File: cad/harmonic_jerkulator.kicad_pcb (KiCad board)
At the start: 2 copper layers, 91 x 87 mm, 43 parts, among them J101 JACK_IN, J102 JACK_OUT, J103 CONN_PSU, J105 PNP, J106 NPN, J107 SW_BYPASS, J108 DIODE1, J109 SW_DIODE, J110 DIODE2, J111 CONN_CONN_BOARD, J112 SW_DIODE, J113 CONN_CIRCUIT_BOARD, K101 TQ2SA-5V, Q101 BC850, Q102 BC856, Q103 DTC123Y, Q104 DTC123Y, U101 4013

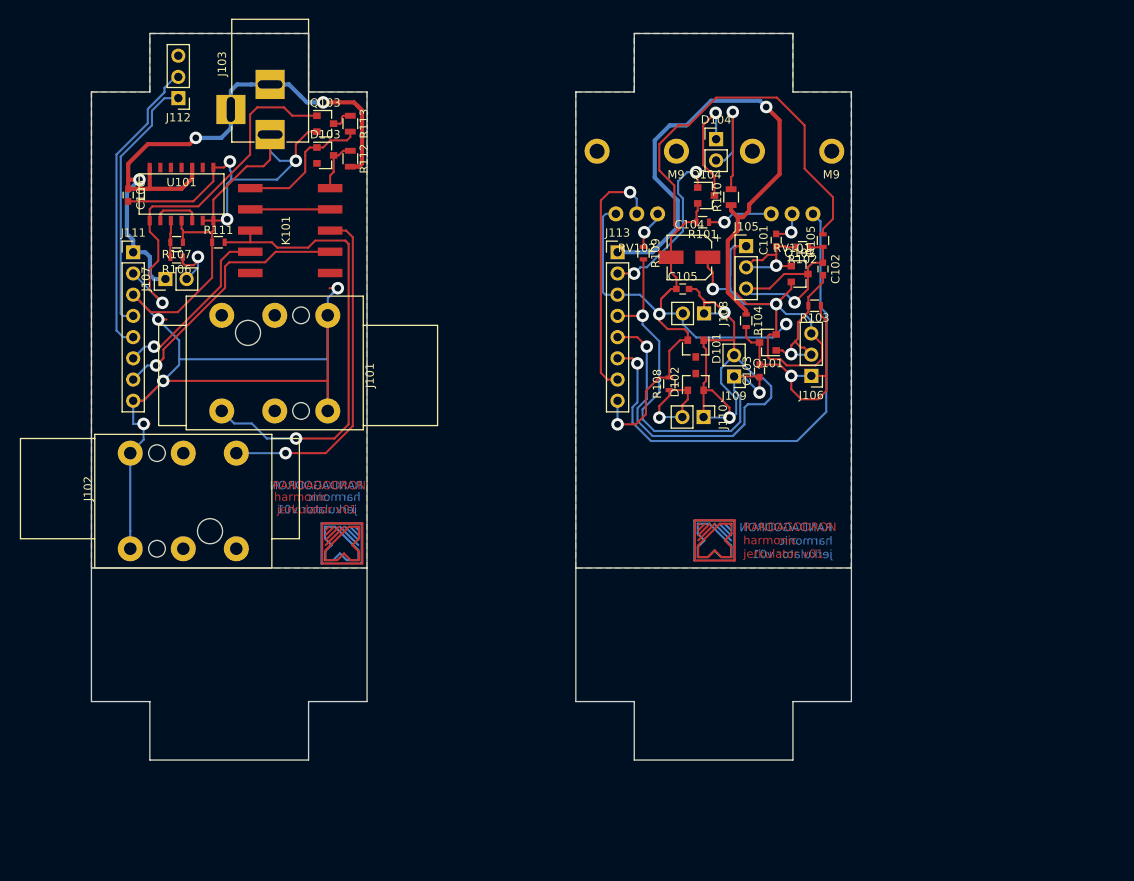
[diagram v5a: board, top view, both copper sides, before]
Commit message: Done corrections, issues #1 to #6.
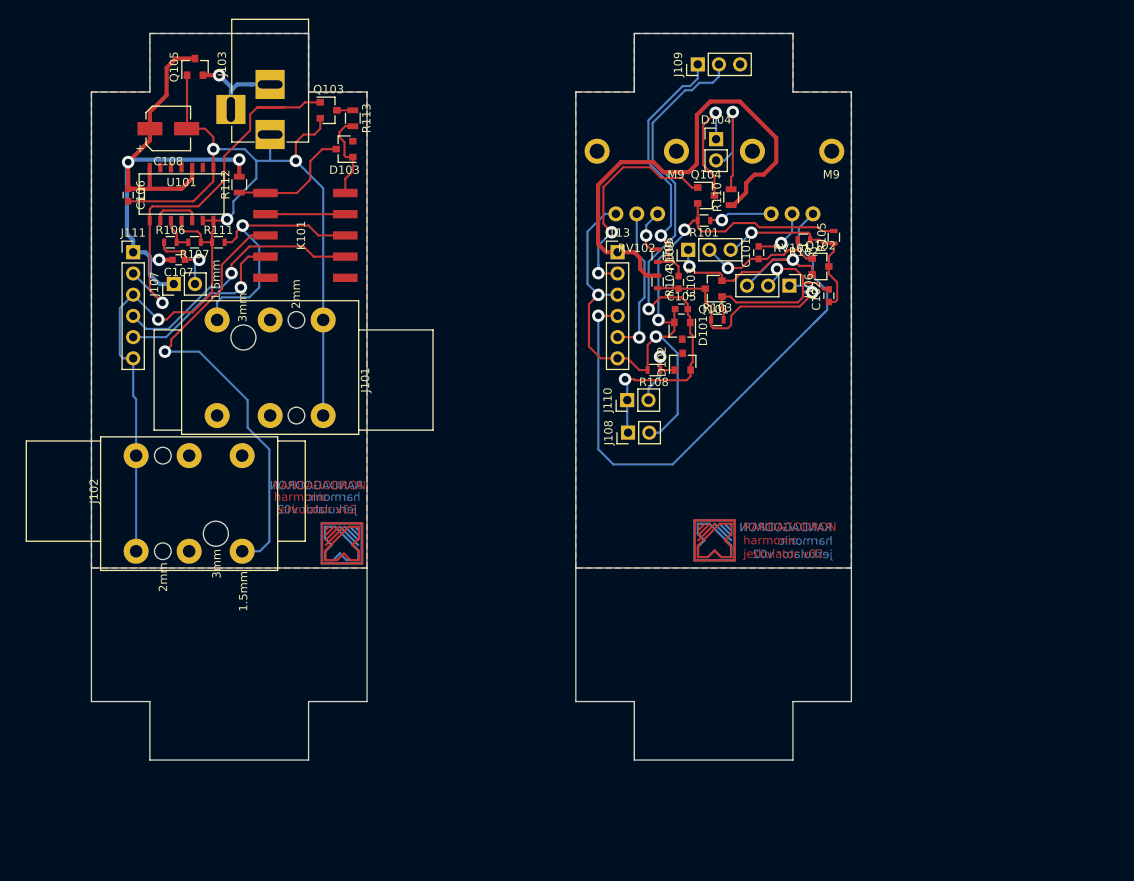
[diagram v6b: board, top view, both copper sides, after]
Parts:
- removed C104: 22u, Capacitors_SMD:CP_Elec_5x5.3
- removed J112: SW_DIODE, Pin_Headers:Pin_Header_Straight_1x03_Pitch2.54mm
- added C107: 100n, Capacitors_SMD:C_0603, F.Cu at (74.5, 73.1)
- added C108: 22u, Capacitors_SMD:CP_Elec_5x5.3, F.Cu at (73.2, 57.4)
- added Q105: DTA114E, TO_SOT_Packages_SMD:SOT-23, F.Cu at (76.4, 50.0)
- J109: value SW_DIODE -> DIODE_SW; footprint Pin_Headers:Pin_Header_Straight_1x02_Pitch2.54mm -> Pin_Headers:Pin_Header_Straight_1x03_Pitch2.54mm
- J111: value CONN_CONN_BOARD -> Conn_01x06; footprint Pin_Headers:Pin_Header_Straight_1x08_Pitch2.54mm -> Pin_Headers:Pin_Header_Straight_1x06_Pitch2.54mm
- J113: value CONN_CIRCUIT_BOARD -> Conn_01x06; footprint Pin_Headers:Pin_Header_Straight_1x08_Pitch2.54mm -> Pin_Headers:Pin_Header_Straight_1x06_Pitch2.54mm
- moved J109 37.6 mm to (136.6, 49.7), turned to 90 degrees
- moved J108 16.9 mm to (128.3, 93.8), turned to 90 degrees
- moved C103 14.4 mm to (134.3, 75.8), turned to 270 degrees
- moved R112 13.7 mm to (81.7, 64.1), turned to 90 degrees
- moved R103 11.8 mm to (138.9, 80.3), turned to 0 degrees
- moved R104 11.6 mm to (131.8, 75.8)
- moved J106 11.1 mm to (147.6, 76.2), turned to 270 degrees
- moved J110 9.36 mm to (128.2, 89.9), turned to 90 degrees
- moved Q101 9.16 mm to (138.5, 76.5)
- moved J105 6.95 mm to (135.5, 71.9), turned to 90 degrees
- moved C102 3.28 mm to (152.3, 77.4), turned to 90 degrees
- moved D102 2.88 mm to (134.8, 85.3)
- moved D101 2.67 mm to (134.8, 81.6)
- moved Q102 2.66 mm to (151.3, 73.9)
- moved C101 2.58 mm to (143.9, 72.2)
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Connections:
- J103 pad 2: VDD -> Net-(J103-Pad2)
- J103 pad 3: VDD -> Net-(J103-Pad2)
- J111 pad 4: /SW_DIODE_1A -> /FX_IN_A
- J111 pad 5: /SW_DIODE_2A -> /FX_OUT_A
- J111 pad 6: /FX_IN_A -> GND
- J113 pad 4: /SW_DIODE_1B -> /FX_IN_B
- J113 pad 5: /SW_DIODE_2B -> /FX_OUT_B
- J113 pad 6: /FX_IN_B -> GNDD
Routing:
- net GND: track 199.4 -> 150.1 mm, vias 7 -> 4
- net Net-(C104-Pad1): track 63.9 -> 26.9 mm
- net GNDD: track 126.7 -> 90.7 mm, vias 3 -> 4
- net /SW_DIODE_2A: track 36.0 -> 0.00 mm
- net /SW_DIODE_1A: track 31.2 -> 0.00 mm
- net /AUDIO_IN: track 56.9 -> 32.3 mm
- net /SW_DIODE_2B: track 89.7 -> 65.7 mm, vias 3 -> 2
- net /SW_DIODE_1B: track 51.1 -> 32.5 mm, vias 2 -> 1
- net /AUDIO_OUT: track 40.9 -> 54.0 mm
- net /FX_OUT_B: track 29.8 -> 18.1 mm
- net Net-(J103-Pad2): track 0.00 -> 11.5 mm, vias 0 -> 1
- net /FX_OUT_A: track 32.0 -> 21.5 mm
- net /FX_IN_A: track 21.1 -> 31.6 mm
- net /FX_IN_B: track 59.9 -> 70.1 mm
- net Net-(D103-Pad3): track 6.32 -> 15.1 mm
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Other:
- board text added: "RANDAGODRON harmonic jerkulator v02"
- board text added: "jerkulator v02"
- board text removed: "RANDAGODRON harmonic jerkulator v01"
- board text removed: "jerkulator v01"

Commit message: Changed PSU connector. Corrected layout.
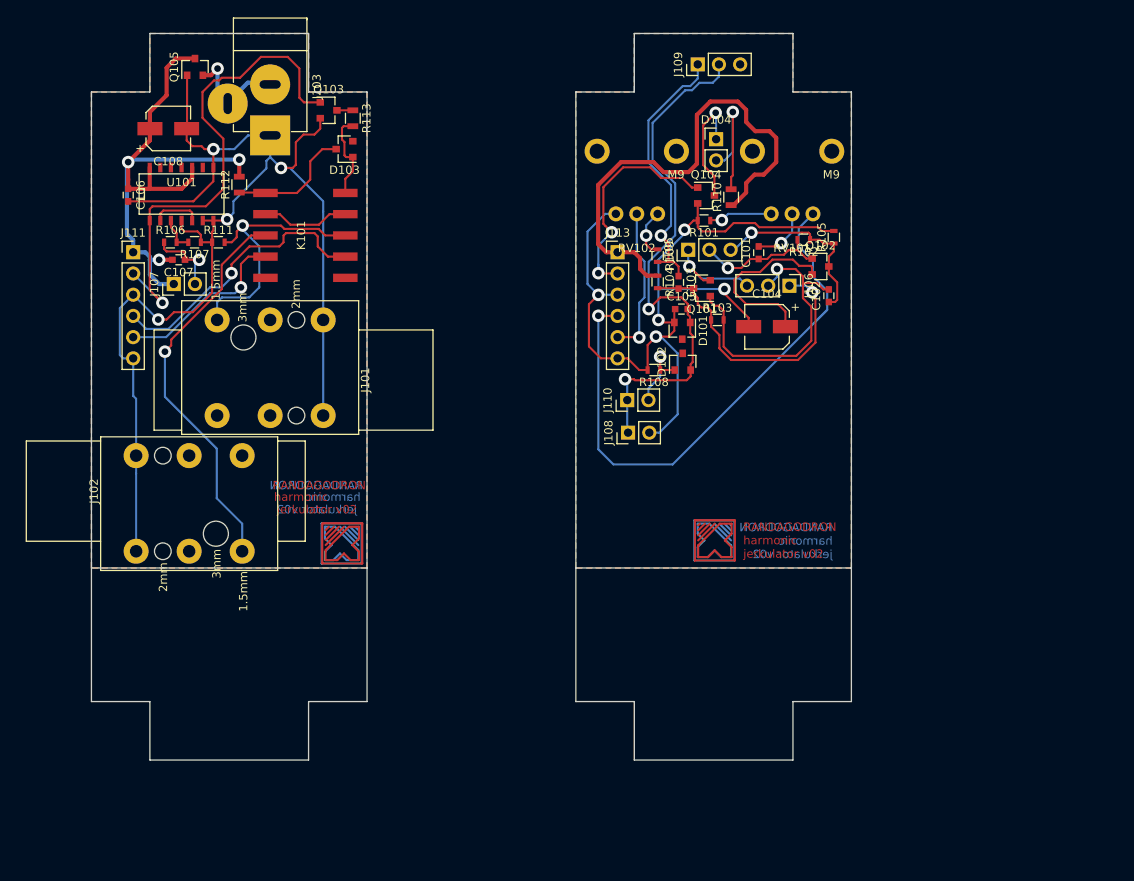
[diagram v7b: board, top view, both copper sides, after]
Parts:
- added C104: 22u, Capacitors_SMD:CP_Elec_5x5.3, F.Cu at (144.9, 81.1)
- J103: footprint Connect:BARREL_JACK -> Connect:JACK_ALIM
- moved Q101 1.40 mm to (137.1, 76.5)
- moved J103 0.10 mm to (85.4, 58.2)
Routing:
- net GNDD: track 90.7 -> 104.3 mm, vias 4 -> 5
- net Net-(C102-Pad2): track 25.0 -> 37.0 mm
- net /BYPASS_CMD: track 48.5 -> 59.4 mm
- net Net-(C104-Pad1): track 26.9 -> 35.0 mm, vias 2 -> 1
- net Net-(C103-Pad2): track 28.3 -> 35.5 mm
- net /AUDIO_OUT: track 54.0 -> 47.6 mm
- net GND: track 150.1 -> 154.3 mm
- net Net-(J103-Pad2): track 11.5 -> 15.0 mm
- net /FX_IN_A: track 31.6 -> 34.1 mm
- net Net-(K101-Pad2): track 9.56 -> 10.6 mm
- net VAA: track 59.3 -> 60.2 mm

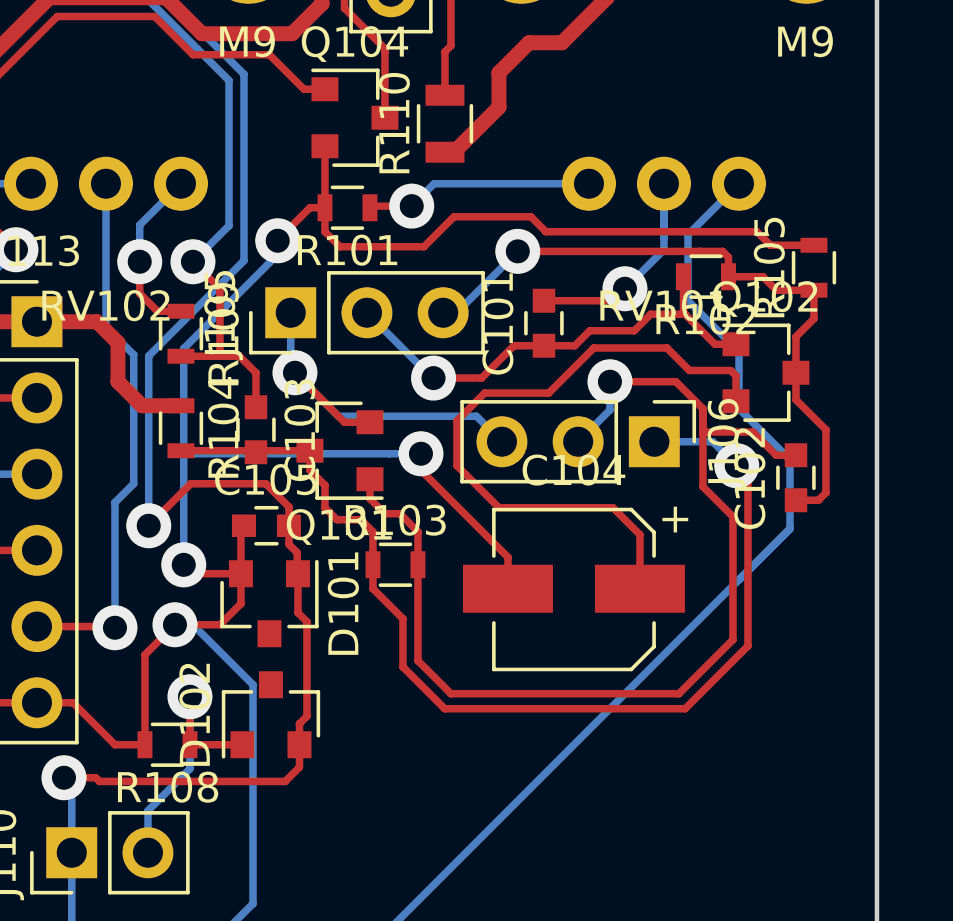
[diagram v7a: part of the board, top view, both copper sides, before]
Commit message: Corrected unconnected net.
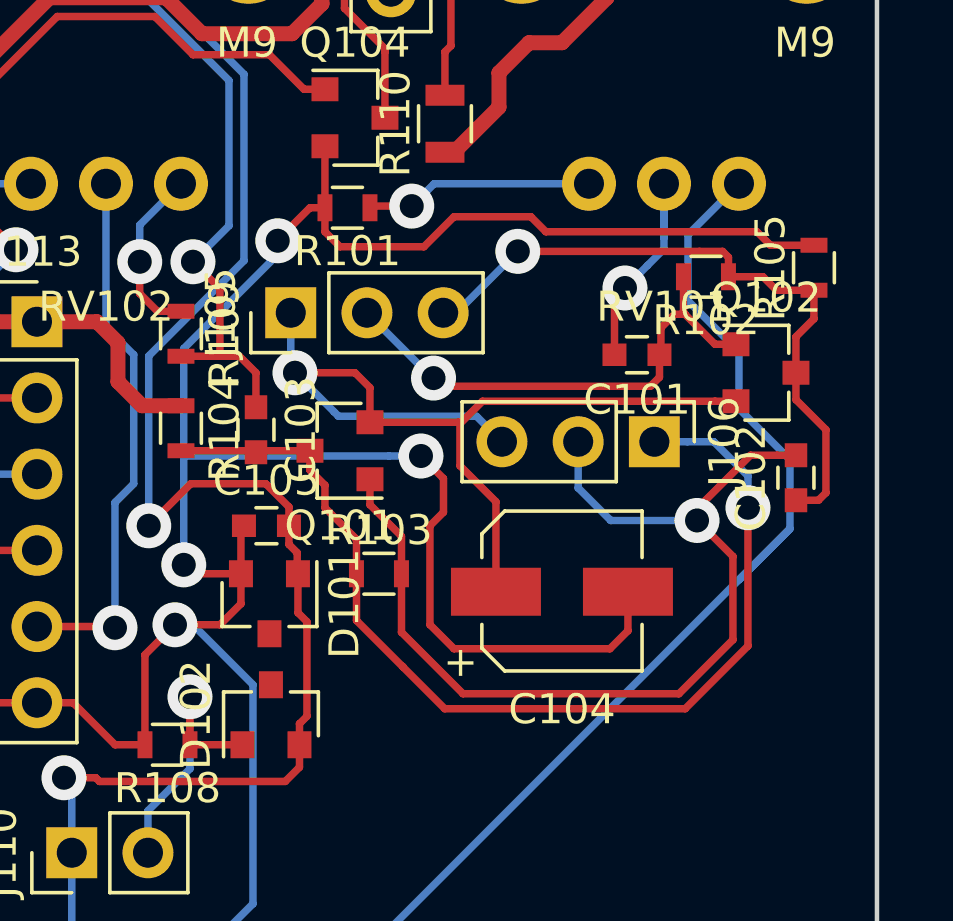
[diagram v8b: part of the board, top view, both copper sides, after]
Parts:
- moved C101 3.27 mm to (147.0, 73.3), turned to 180 degrees
- moved R103 0.63 mm to (138.4, 80.6)
- moved C104 0.41 mm to (144.5, 81.2), turned to 0 degrees
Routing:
- net GNDD: track 104.3 -> 113.2 mm
- net Net-(C102-Pad2): track 37.0 -> 33.0 mm
- net Net-(C104-Pad1): track 35.0 -> 32.4 mm
- net Net-(C101-Pad1): track 15.9 -> 17.1 mm
- net Net-(C101-Pad2): track 8.70 -> 8.18 mm
